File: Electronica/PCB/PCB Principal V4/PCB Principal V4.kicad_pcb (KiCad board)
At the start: 2 copper layers, 126.1 x 70 mm, 16 parts, among them J2 Power Monster

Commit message: Listo PCB Botones
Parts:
- added D3: LED, LED_THT:LED_D5.0mm_Horizontal_O1.27mm_Z3.0mm, F.Cu at (28.4, 91.2)
- added D4: LED, LED_THT:LED_D5.0mm_Horizontal_O1.27mm_Z3.0mm, B.Cu at (119.1, 77.8)
- added R1: 220, Resistor_THT:R_Axial_DIN0204_L3.6mm_D1.6mm_P5.08mm_Horizontal, F.Cu at (54.9, 91.0)
- added R2: 220, Resistor_THT:R_Axial_DIN0204_L3.6mm_D1.6mm_P5.08mm_Horizontal, F.Cu at (115.7, 74.0)
- moved Switch Motores 3.05 mm to (124.3, 78.8)
- moved J2 2.66 mm to (106.6, 77.8)
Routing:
- net MOTORES: track 132.7 -> 123.3 mm
- net Net-(J2-Pin_2): track 6.86 -> 0.00 mm
- net GND: track 375.9 -> 379.0 mm
- net +5V: track 182.8 -> 180.3 mm

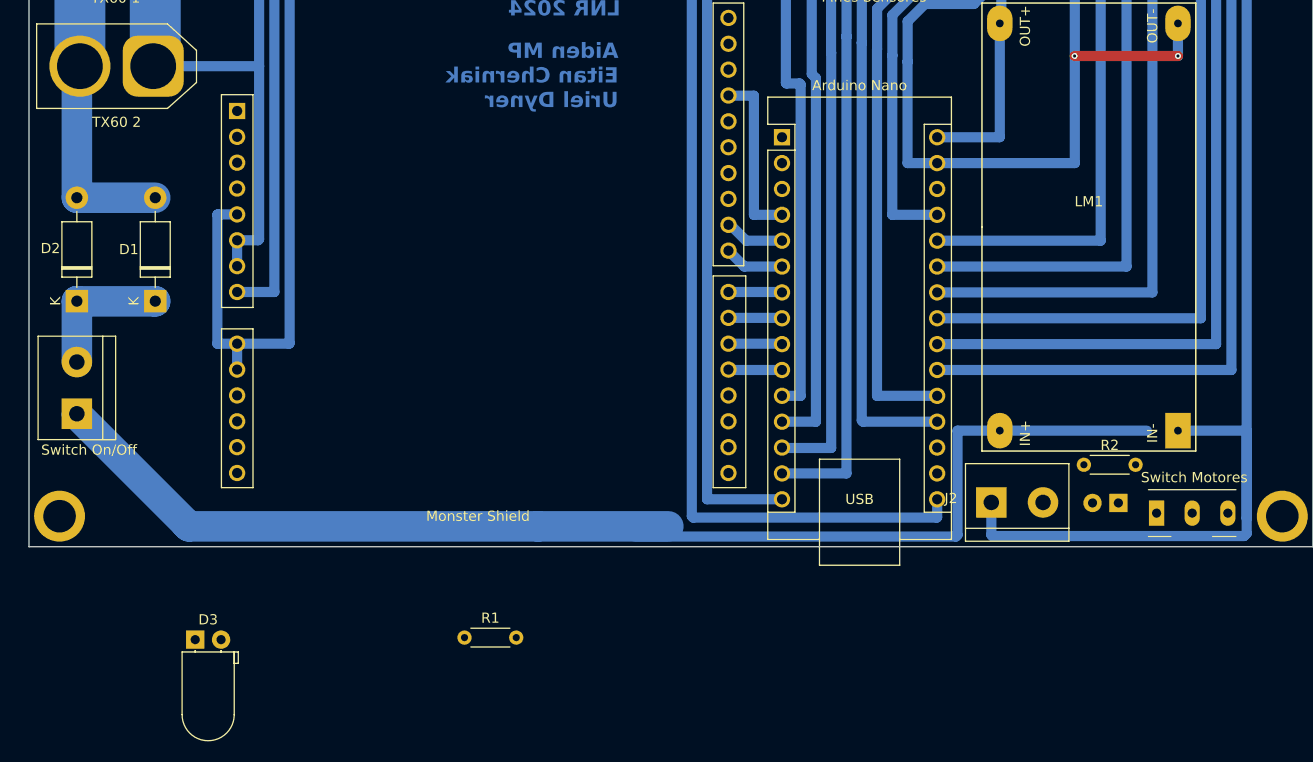
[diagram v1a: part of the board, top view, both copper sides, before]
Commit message: PCB Principal con leds
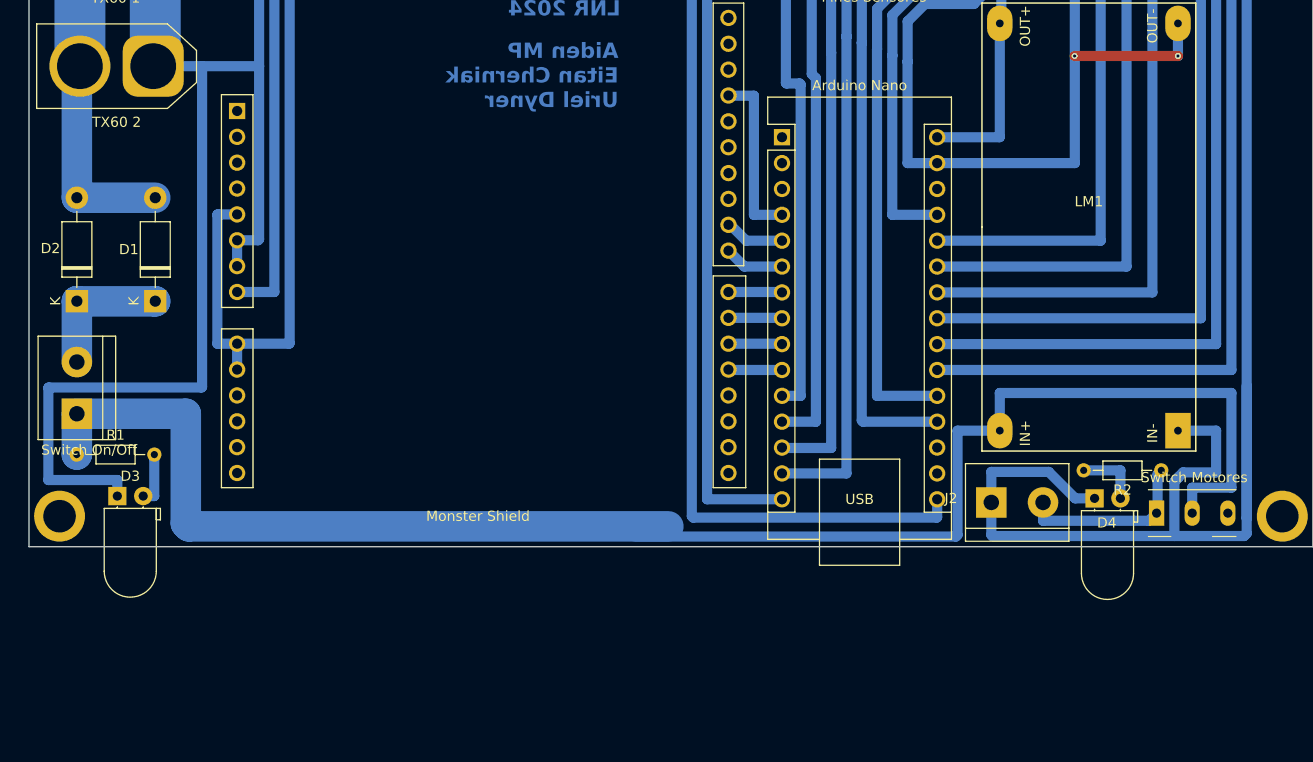
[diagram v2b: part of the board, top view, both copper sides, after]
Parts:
- D4: moved to F.Cu
- R1, R2: footprint Resistor_THT:R_Axial_DIN0204_L3.6mm_D1.6mm_P5.08mm_Horizontal -> Resistor_THT:R_Axial_DIN0204_L3.6mm_D1.6mm_P7.62mm_Horizontal
- moved R1 42.1 mm to (16.8, 73.0)
- moved D3 16.0 mm to (20.8, 77.1)
- moved R2 7.62 mm to (123.3, 74.6), turned to 180 degrees
- moved D4 2.38 mm to (116.8, 77.3), turned to 0 degrees
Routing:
- net GND: track 379.0 -> 472.6 mm
- net MOTORES: track 123.3 -> 161.3 mm
- net Net-(J2-Pin_2): track 0.00 -> 17.7 mm
- net Net-(D4-A): track 0.00 -> 6.36 mm
- net Net-(D3-A): track 0.00 -> 5.56 mm

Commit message: TEST POINTSSSS
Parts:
- added 5V: Conn_01x01, Connector_PinHeader_1.00mm:PinHeader_1x01_P1.00mm_Vertical, F.Cu at (25.8, 15.1)
- added GND: Conn_01x01, Connector_PinHeader_1.00mm:PinHeader_1x01_P1.00mm_Vertical, F.Cu at (22.7, 15.1)
- added PIN+: Conn_01x01, Connector_PinHeader_1.00mm:PinHeader_1x01_P1.00mm_Vertical, F.Cu at (19.3, 15.1)
- added VIN: Conn_01x01, Connector_PinHeader_1.00mm:PinHeader_1x01_P1.00mm_Vertical, F.Cu at (28.5, 15.1)
- SW Motores: renamed from Switch Motores
- SW On/Off: renamed from Switch On/Off
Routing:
- net +5V: track 180.3 -> 193.9 mm, vias 2 -> 4
- net VIN: track 145.4 -> 154.2 mm, vias 0 -> 2
- net Net-(D1-A): track 33.4 -> 41.9 mm
- net GND: track 472.6 -> 480.9 mm

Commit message: Codigo nuevo sin terminar
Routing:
- net VIN: track 154.2 -> 167.2 mm
- net GND: track 480.9 -> 492.8 mm, vias 2 -> 4
- net +5V: track 193.9 -> 204.7 mm
- net CNY 1: track 53.0 -> 48.3 mm
- net CNY 2: track 49.3 -> 45.2 mm
- net ECHO 1: track 56.5 -> 52.9 mm
- net TRIG 1: track 52.0 -> 49.2 mm
- net LED4: track 74.2 -> 76.8 mm
- net TRIG 3: track 97.6 -> 99.5 mm
- net LED3: track 85.2 -> 87.2 mm
- net MOTORES: track 161.3 -> 159.4 mm
- net ECHO 2: track 47.9 -> 46.2 mm
- net LED2: track 96.4 -> 97.7 mm
- net ECHO 3: track 69.7 -> 70.7 mm
- net TRIG 2: track 45.0 -> 44.1 mm

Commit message: PCB Principal V5 (sin terminar)
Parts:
- removed 5V, GND, PIN+, VIN: Conn_01x01, Connector_PinHeader_1.00mm:PinHeader_1x01_P1.00mm_Vertical
- removed IDC Botones/Leds: IDC Placa Botones, Connector_IDC:IDC-Header_2x05_P2.54mm_Horizontal
- removed TX60 1: Power Input 2, Connector_AMASS:AMASS_XT60-M_1x02_P7.20mm_Vertical
- removed TX60 2: Power Input 1, Connector_AMASS:AMASS_XT60-M_1x02_P7.20mm_Vertical
- added ?: , , F.Cu at (155.3, 166.7)
- added ?: , , F.Cu at (35.2, 102.7)
- added ?: , , F.Cu at (35.2, 166.7)
- added ?: , , F.Cu at (155.3, 102.7)
- added Arduino Nano: Arduino_Nano_v3.x, Module:Arduino_Nano, F.Cu at (212.0, 34.0)
- added D1: 1N4007, Diode_THT:D_DO-41_SOD81_P10.16mm_Horizontal, F.Cu at (187.2, 65.2)
- added D2: 1N4007, Diode_THT:D_DO-41_SOD81_P10.16mm_Horizontal, F.Cu at (187.2, 68.8)
- added D3: LED, LED_THT:LED_D5.0mm_Horizontal_O1.27mm_Z3.0mm, F.Cu at (164.7, 70.3)
- added D4: LED, LED_THT:LED_D5.0mm_Horizontal_O1.27mm_Z3.0mm, F.Cu at (243.9, 71.2)
- added J12: TP, Connector_PinHeader_2.54mm:PinHeader_1x05_P2.54mm_Vertical, F.Cu at (20.0, 15.2)
- added J12: TP, Connector_PinHeader_2.54mm:PinHeader_1x05_P2.54mm_Vertical, F.Cu at (172.6, 68.8)
- added J2: Power Monster, TerminalBlock:TerminalBlock_bornier-2_P5.08mm, F.Cu at (232.2, 71.6)
- added J4: Power Input 2, Connector_AMASS:AMASS_XT60-M_1x02_P7.20mm_Vertical, F.Cu at (24.6, 34.9)
- added J4: Power Input 2, Connector_AMASS:AMASS_XT60-M_1x02_P7.20mm_Vertical, F.Cu at (200.6, 52.0)
- added J5: IDC Placa Botones, Connector_PinHeader_2.54mm:PinHeader_2x05_P2.54mm_Horizontal, F.Cu at (236.8, -3.80)
- added J5: IDC Placa Botones, Connector_PinHeader_2.54mm:PinHeader_2x05_P2.54mm_Horizontal, F.Cu at (114.8, 25.8)
- added J6: Power Input 1, Connector_AMASS:AMASS_XT60-M_1x02_P7.20mm_Vertical, F.Cu at (182.6, 51.8)
- added J6: Power Input 1, Connector_AMASS:AMASS_XT60-M_1x02_P7.20mm_Vertical, F.Cu at (24.8, 24.3)
- added LM1: LM2596_OK, LM2596:LM2596_correctedMeas, F.Cu at (241.8, 44.5)
- added Monster Shield: MONSTER SHIELD, Module:Arduino_UNO_R3, B.Cu at (155.6, 0.07)
- added Pines Sensores: Conexion Sensores, Connector_PinHeader_2.54mm:PinHeader_2x08_P2.54mm_Horizontal, F.Cu at (213.8, -3.75)
- added R1: 220, Resistor_THT:R_Axial_DIN0204_L3.6mm_D1.6mm_P7.62mm_Horizontal, F.Cu at (162.3, 67.2)
- added R2: 220, Resistor_THT:R_Axial_DIN0204_L3.6mm_D1.6mm_P7.62mm_Horizontal, F.Cu at (249.2, 68.5)
- added SW Motores: On/Off Motores, Button_Switch_THT:SW_Slide_SPDT_Angled_CK_OS102011MA1Q, F.Cu at (254.6, 71.1)
- added SW On/Off: On/Off General, TerminalBlock:TerminalBlock_bornier-2_P5.08mm, F.Cu at (203.3, 69.2)
- moved D1 2.16 mm to (24.4, 60.1)
- moved D2 2.16 mm to (16.6, 60.1)
- moved R1 0.80 mm to (16.8, 73.8)
- moved SW On/Off 0.80 mm to (16.8, 69.8)
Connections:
- net Net-(D1-A) renamed PI+
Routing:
- net GND: track 492.8 -> 444.9 mm, vias 4 -> 6
- net PI+: track 41.9 -> 7.70 mm
- net +5V: track 204.7 -> 194.3 mm, vias 4 -> 6
- net Net-(D1-K): track 13.7 -> 6.04 mm
- net VIN: track 167.2 -> 162.7 mm, vias 2 -> 4
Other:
- board size 126.1 x 70 mm -> 146.2 x 157.6 mm

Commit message: -
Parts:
- removed the ? at (155.3, 166.7)
- removed the ? at (35.2, 102.7)
- removed the ? at (35.2, 166.7)
- removed the ? at (155.3, 102.7)
- removed the Arduino Nano at (212.0, 34.0)
- removed the D1 at (187.2, 65.2)
- removed the D2 at (187.2, 68.8)
- removed the D3 at (164.7, 70.3)
- removed the D4 at (243.9, 71.2)
- removed the J12 at (172.6, 68.8)
- removed the J2 at (232.2, 71.6)
- removed the J4 at (200.6, 52.0)
- removed the J5 at (236.8, -3.80)
- removed the J6 at (182.6, 51.8)
- removed the LM1 at (241.8, 44.5)
- removed the Monster Shield at (155.6, 0.07)
- removed the Pines Sensores at (213.8, -3.75)
- removed the R1 at (162.3, 67.2)
- removed the R2 at (249.2, 68.5)
- removed the SW Motores at (254.6, 71.1)
- removed the SW On/Off at (203.3, 69.2)
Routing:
- net VIN: vias 4 -> 2
- net GND: vias 6 -> 4
- net +5V: vias 6 -> 4
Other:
- board size 146.2 x 157.6 mm -> 126.1 x 70 mm
